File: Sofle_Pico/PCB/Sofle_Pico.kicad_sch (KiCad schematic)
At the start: 107 parts, among them J1 Conn_01x05, J2 MJ-4PP-9, J3 Conn_01x04, J4 Conn_01x04, J5 Conn_01x05, J6 Conn_01x05, SW1 SW_PUSH_LED, SW10 SW_PUSH_LED, SW11 SW_PUSH_LED, SW12 SW_PUSH_LED, SW13 SW_PUSH_LED, SW14 SW_PUSH_LED, SW15 SW_PUSH_LED, SW16 SW_PUSH_LED, SW17 SW_PUSH_LED, SW18 SW_PUSH_LED, SW19 SW_PUSH_LED, SW2 SW_PUSH_LED, SW20 SW_PUSH_LED, SW21 SW_PUSH_LED, SW22 SW_PUSH_LED, SW23 SW_PUSH_LED, SW24 SW_PUSH_LED, SW25 Rotary_Encoder_Switch-Device, SW26 SW_PUSH_LED, SW27 SW_PUSH_LED, SW28 SW_PUSH_LED, SW29 SW_PUSH_LED, SW3 SW_PUSH_LED, SW30 SW_PUSH_LED, SW4 SW_PUSH_LED, SW5 SW_PUSH_LED, SW6 SW_PUSH_LED, SW7 SW_PUSH_LED, SW8 SW_PUSH_LED, SW9 SW_PUSH_LED, U1 SN74AHCT1G125, U3 Pico

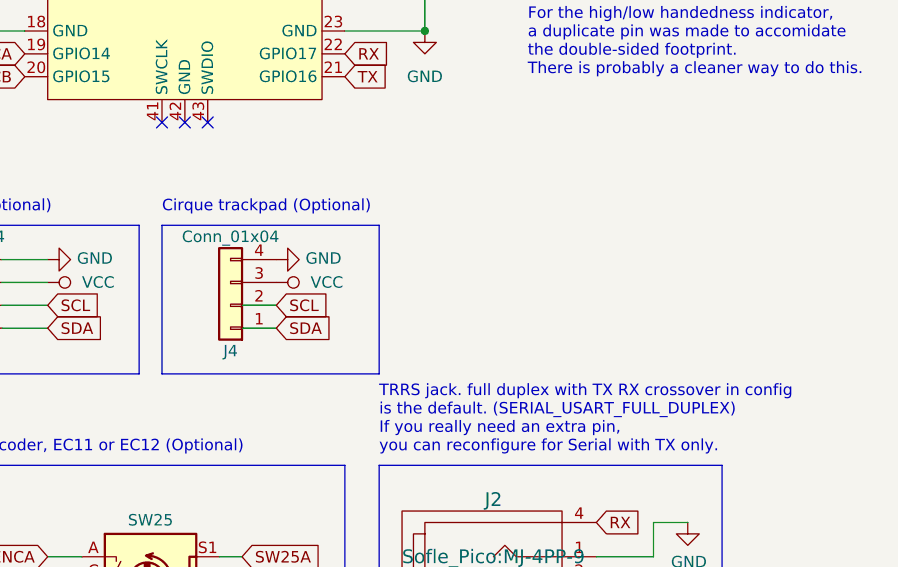
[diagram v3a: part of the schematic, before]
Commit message: Added LH Cirque trackpad tie in Updated keyplate outline for trackpad tie in Fixed flipped switch 1
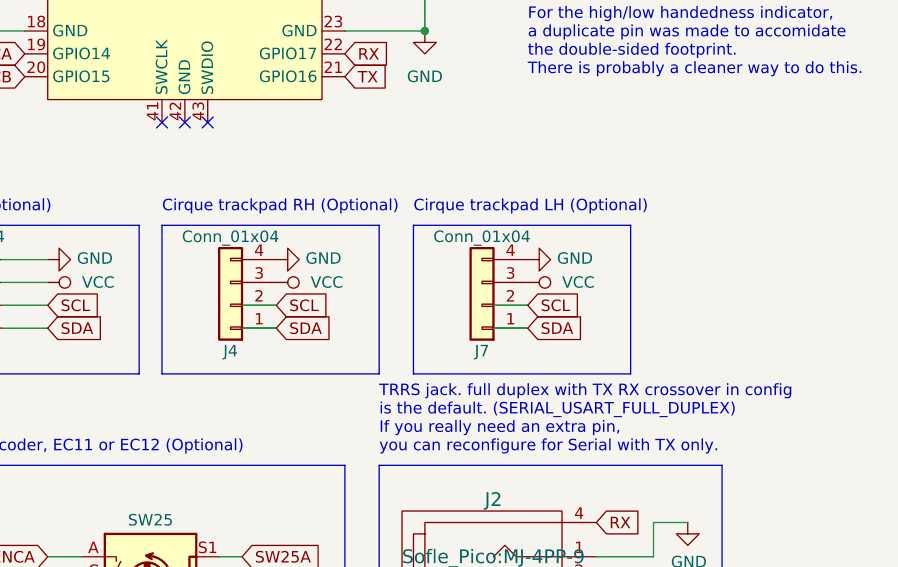
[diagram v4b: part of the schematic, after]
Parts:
- added J7: Conn_01x04, Sofle_Pico:Cirque tie in, symbol Sofle_Pico:Conn_01x04
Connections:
- net GND: now also J7.4 (Pin_4)
- net SCL: now also J7.2 (Pin_2)
- net SDA: now also J7.1 (Pin_1)
- net VCC: now also J7.3 (Pin_3)
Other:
- note added: "Cirque trackpad LH (Optional)"
- note added: "Cirque trackpad RH (Optional)"
- note removed: "Cirque trackpad (Optional)"
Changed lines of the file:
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@@
     (stroke (width 0) (type default))
   )
+  (wire (pts (xy 78.74 102.87) (xy 82.55 102.87))
+    (stroke (width 0) (type default))
+  )
   (wire (pts (xy 185.42 41.91) (xy 185.42 45.72))
     (stroke (width 0) (type default))
@@
     (stroke (width 0) (type default))
   )
+  (wire (pts (xy 78.74 100.33) (xy 82.55 100.33))
+    (stroke (width 0) (type default))
+  )
   (wire (pts (xy 179.07 130.81) (xy 199.39 130.81))
     (stroke (width 0) (type default))
@@
     (fill (type none))
   )
+  (rectangle (start 69.85 91.44) (end 93.98 107.95)
+    (stroke (width 0) (type default))
+    (fill (type none))
+  )
   (rectangle (start 50.8 60.96) (end 101.6 66.04)
     (stroke (width 0) (type default))
@@
     (fill (type none))
   )
-  (text "Cirque trackpad (Optional)\n" (at 41.91 90.17 0)
+  (text "Cirque trackpad RH (Optional)\n" (at 41.91 90.17 0)
     (effects (font (size 1.27 1.27)) (justify left bottom))
   )
@@
     (effects (font (size 1.27 1.27)) (justify left bottom))
   )
+  (text "Cirque trackpad LH (Optional)\n" (at 69.85 90.17 0)
+    (effects (font (size 1.27 1.27)) (justify left bottom))
+  )
   (text "Notes:\nPiezzo speaker not supported for this \nboard without _considerable_ effort. \nInntentionaly removed.\nSolenoid also removed. (It needs v5, Pico is 3.3)"
     (at 15.24 186.69 0)
@@
     )
   )
+  (global_label "SDA" (shape input) (at 82.55 102.87 0)
+    (effects (font (size 1.27 1.27)) (justify left))
+    (property "Intersheetrefs" "${INTERSHEET_REFS}" (at 82.55 102.87 0)
+      (effects (font (size 1.27 1.27)) hide)
+    )
+  )
   (global_label "row3" (shape input) (at 26.67 59.69 180)
     (effects (font (size 1.27 1.27)) (justify right))
@@
     )
   )
+  (global_label "SCL" (shape input) (at 82.55 100.33 0)
+    (effects (font (size 1.27 1.27)) (justify left))
+    (property "Intersheetrefs" "${INTERSHEET_REFS}" (at 82.55 100.33 0)
+      (effects (font (size 1.27 1.27)) hide)
+    )
+  )
   (global_label "col5" (shape input) (at 143.51 90.17 90)
     (effects (font (size 1.27 1.27)) (justify left))
@@
     )
   )
+  (symbol (lib_id "SofleKeyboard-rescue:VCC-power") (at 82.55 97.79 270) (unit 1)
+    (in_bom yes) (on_board yes) (dnp no)
+    (property "Reference" "#PWR025" (at 78.74 97.79 0)
+      (effects (font (size 1.27 1.27)) hide)
+    )
+    (property "Value" "VCC" (at 86.36 97.79 90)
+      (effects (font (size 1.27 1.27)) (justify left))
+    )
+    (property "Footprint" "" (at 82.55 97.79 0)
+      (effects (font (size 1.27 1.27)) hide)
+    )
+    (property "Datasheet" "" (at 82.55 97.79 0)
+      (effects (font (size 1.27 1.27)) hide)
+    )
+    (pin "1")
+    (instances
+      (project "Sofle_Pico"
+        (path "/06057b3a-55ab-4f4e-913e-2aeec5ff3587"
+          (reference "#PWR025") (unit 1)
+        )
+      )
+    )
+  )
   (symbol (lib_id "power:GND") (at 64.77 165.1 0) (unit 1)
     (in_bom yes) (on_board yes) (dnp no) (fields_autoplaced)
@@
     )
   )
+  (symbol (lib_id "SofleKeyboard-rescue:GND-power") (at 82.55 95.25 90) (unit 1)
+    (in_bom yes) (on_board yes) (dnp no)
+    (property "Reference" "#PWR024" (at 88.9 95.25 0)
+      (effects (font (size 1.27 1.27)) hide)
+    )
+    (property "Value" "GND" (at 85.8012 95.123 90)
+      (effects (font (size 1.27 1.27)) (justify right))
+    )
+    (property "Footprint" "" (at 82.55 95.25 0)
+      (effects (font (size 1.27 1.27)) hide)
+    )
+    (property "Datasheet" "" (at 82.55 95.25 0)
+      (effects (font (size 1.27 1.27)) hide)
+    )
+    (pin "1")
+    (instances
+      (project "Sofle_Pico"
+        (path "/06057b3a-55ab-4f4e-913e-2aeec5ff3587"
+          (reference "#PWR024") (unit 1)
+        )
+      )
+    )
+  )
   (symbol (lib_id "power:VCC") (at 63.5 153.67 0) (unit 1)
     (in_bom yes) (on_board yes) (dnp no)
@@
         )
       )
+    )
+  )
+  (symbol (lib_id "Sofle_Pico:Conn_01x04") (at 77.47 100.33 180) (unit 1)
+    (in_bom yes) (on_board yes) (dnp no)
+    (property "Reference" "J7" (at 77.47 105.41 0)
+      (effects (font (size 1.27 1.27)))
+    )
+    (property "Value" "Conn_01x04" (at 77.47 92.71 0)
+      (effects (font (size 1.27 1.27)))
+    )
+    (property "Footprint" "Sofle_Pico:Cirque tie in" (at 77.47 100.33 0)
+      (effects (font (size 1.27 1.27)) hide)
+    )
+    (property "Datasheet" "~" (at 77.47 100.33 0)
+      (effects (font (size 1.27 1.27)) hide)
+    )
+    (pin "1")
+    (pin "2")
+    (pin "3")
+    (pin "4")
+    (instances
+      (project "Sofle_Pico"
+        (path "/06057b3a-55ab-4f4e-913e-2aeec5ff3587"
+          (reference "J7") (unit 1)
+        )
+      )

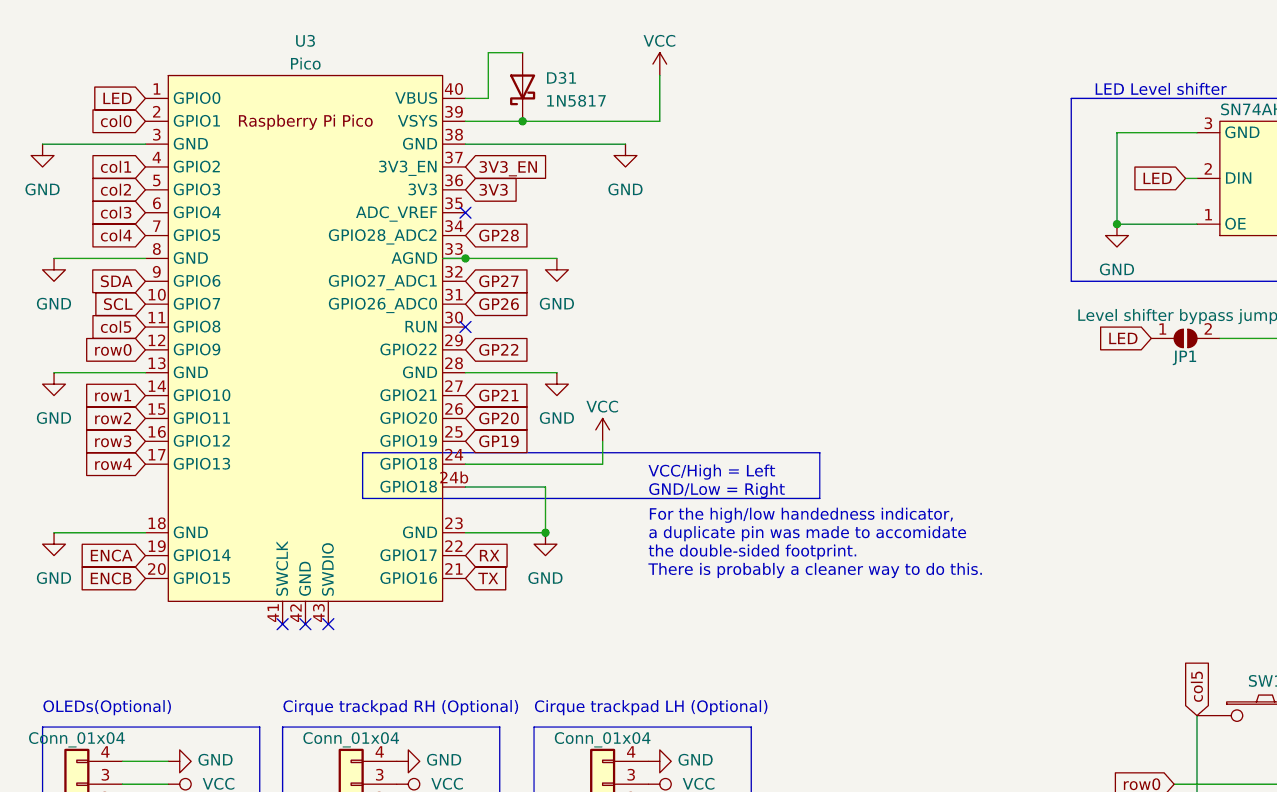
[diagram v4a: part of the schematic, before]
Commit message: Removed handedness pin (I dont want to add pullup resistor)
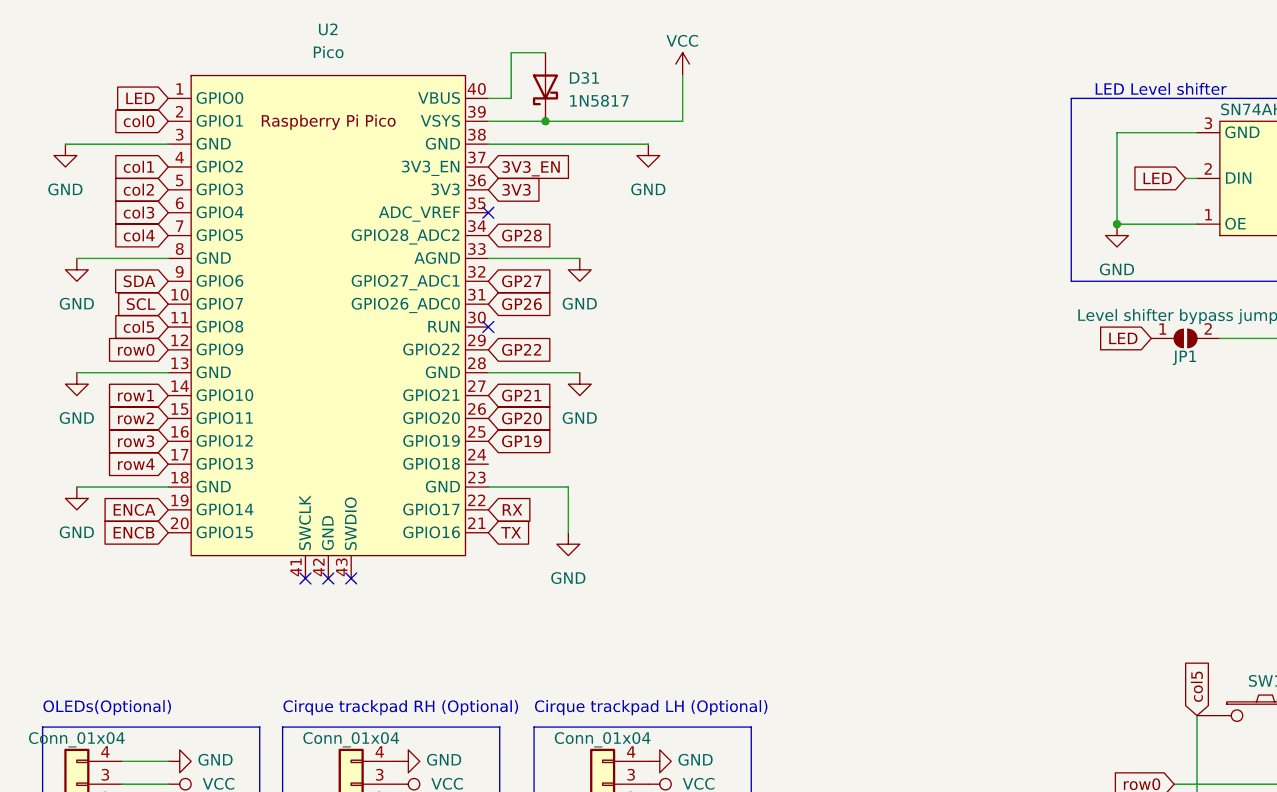
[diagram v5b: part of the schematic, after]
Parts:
- removed U3: Pico, Sofle_Pico:RPi_Pico_SMD_TH-DS Sofle Pico handpins, symbol MCU_RaspberryPi_and_Boards:Pico
- added U2: Pico, Sofle_Pico:RPi_Pico_SMD_TH_DS, symbol Sofle_Pico:Pico
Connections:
- net 3V3: now also U2.36 (3V3)
- net 3V3_EN: now also U2.37 (3V3_EN)
- net ENCA: now also U2.19 (GPIO14)
- net ENCB: now also U2.20 (GPIO15)
- net GND: now also U2.13 (GND), U2.18 (GND), U2.23 (GND), U2.28 (GND), U2.3 (GND), U2.33 (AGND), U2.38 (GND), U2.8 (GND)
- net GP19: now also U2.25 (GPIO19)
- net GP20: now also U2.26 (GPIO20)
- net GP21: now also U2.27 (GPIO21)
- net GP22: now also U2.29 (GPIO22)
- net GP26: now also U2.31 (GPIO26_ADC0)
- net GP27: now also U2.32 (GPIO27_ADC1)
- net GP28: now also U2.34 (GPIO28_ADC2)
- net LED: now also U2.1 (GPIO0)
- net RX: now also U2.22 (GPIO17)
- net SCL: now also U2.10 (GPIO7)
- net SDA: now also U2.9 (GPIO6)
- net SW25A: now also U2.11 (GPIO8)
- net TX: now also U2.21 (GPIO16)
- net VCC: now also U2.39 (VSYS)
- net col0: now also U2.2 (GPIO1)
- net col1: now also U2.4 (GPIO2)
- net col2: now also U2.5 (GPIO3)
- net col3: now also U2.6 (GPIO4)
- net col4: now also U2.7 (GPIO5)
- net row0: now also U2.12 (GPIO9)
- net row1: now also U2.14 (GPIO10)
- net row2: now also U2.15 (GPIO11)
- net row3: now also U2.16 (GPIO12)
- net row4: now also U2.17 (GPIO13)
- net at D31.2 (A): now also U2.40 (VBUS)
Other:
- note removed: "For the high/low handedness indicator, a duplicate pin was made to accomidate the double-sided footprint. There is probably a cleaner way to do this."
- note removed: "VCC/High = Left GND/Low = Right"
